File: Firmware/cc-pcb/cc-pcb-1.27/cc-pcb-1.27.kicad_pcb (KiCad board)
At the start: 2 copper layers, 39.4 x 36.8 mm, 20 parts, among them SW1 SRS

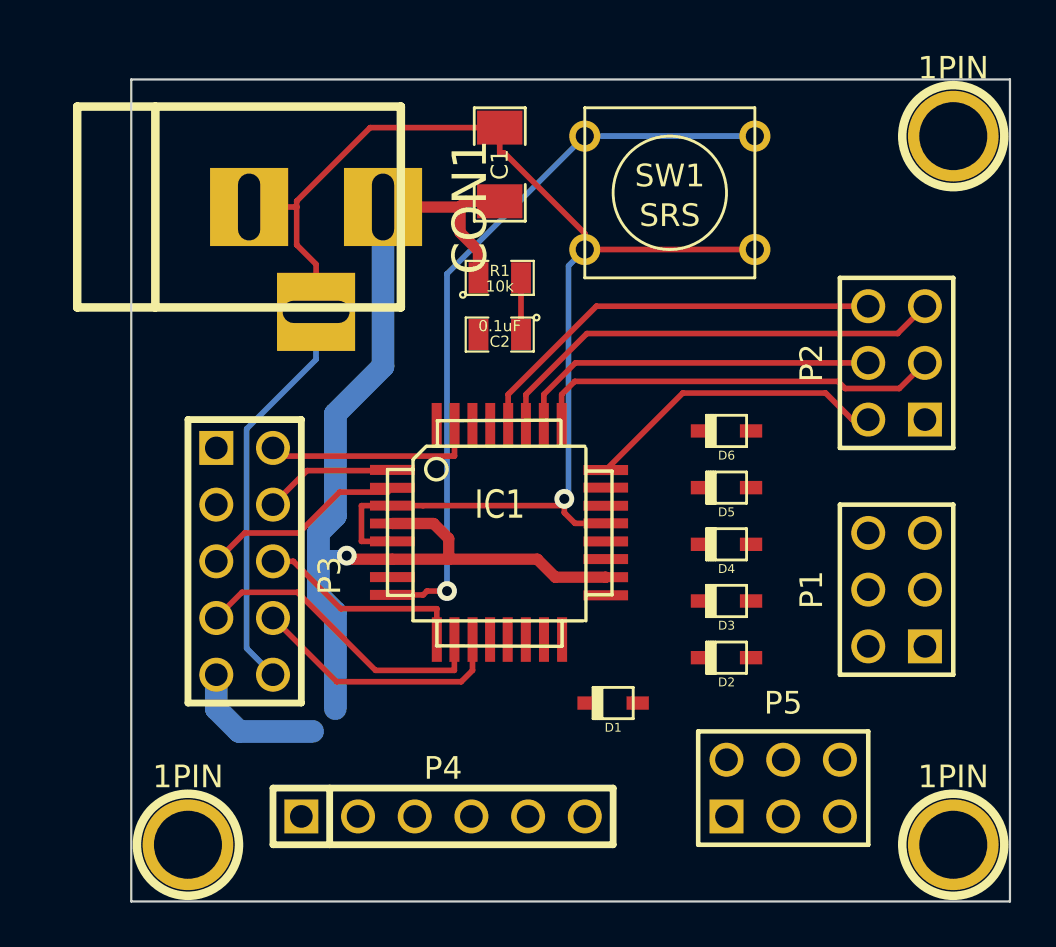
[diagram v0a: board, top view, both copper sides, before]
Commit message: added 1.27 pcb, 2mm pcb
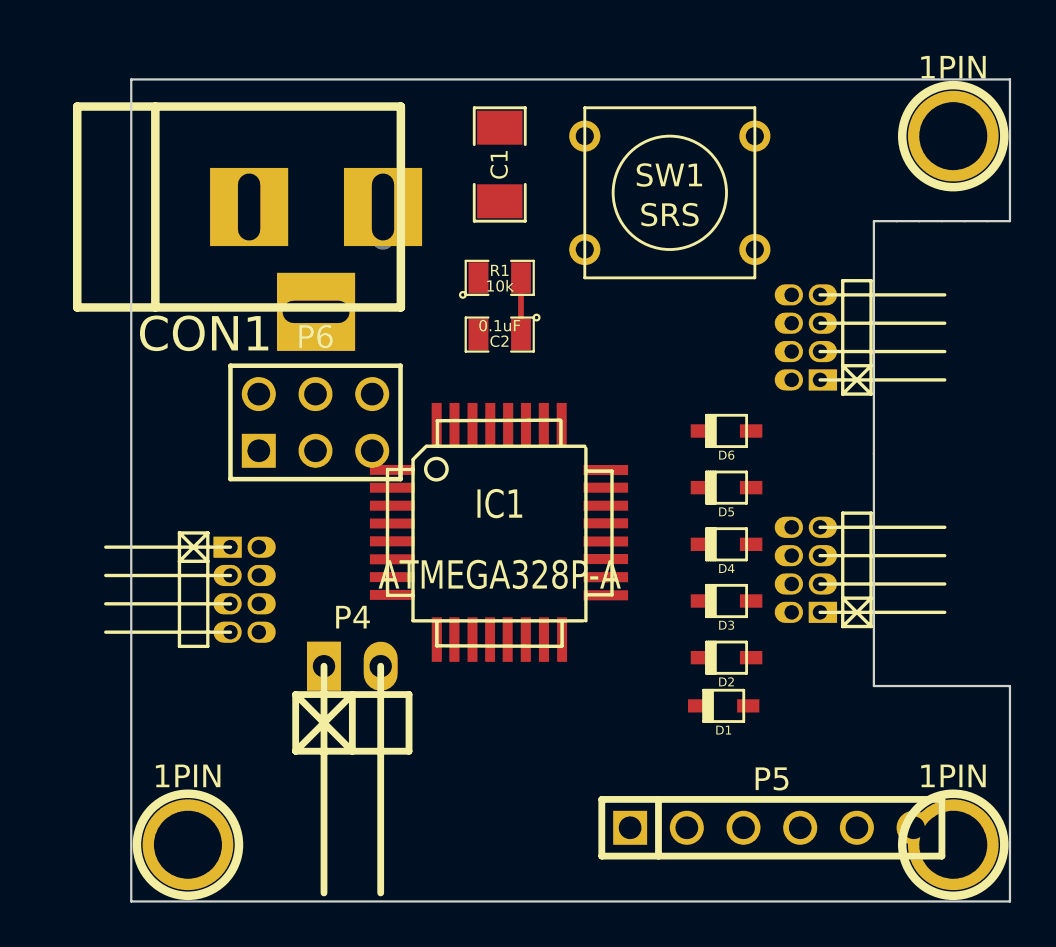
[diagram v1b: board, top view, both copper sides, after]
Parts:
- added P6: CONN_6, pin_array_3x2, F.Cu at (161.9, 87.8)
- CON1: value (none) -> BARREL_JACK
- IC1: value (none) -> ATMEGA328P-A
- P1, P2: value (none) -> CONN_6; footprint pin_array_3x2 -> pin_strip_1.27mm_4x2_90
- P3: value (none) -> CONN_8; footprint PIN_ARRAY_5x2 -> pin_strip_1.27mm_4x2_90
- P4: value (none) -> CONN_2; footprint PIN_ARRAY-6X1 -> pin_strip_2-90
- P5: value (none) -> CONN_6; footprint pin_array_3x2 -> PIN_ARRAY-6X1
- moved P4 7.86 mm to (163.6, 98.7)
- moved D1 4.95 mm to (180.2, 100.5)
- moved P2 4.22 mm to (183.9, 83.9)
- moved P1 4.16 mm to (183.9, 94.4)
- moved P5 1.85 mm to (182.4, 105.9)
- moved P3 1.27 mm to (158.8, 95.2)
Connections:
- C2 pad 1: N-0000029 -> N-000003
- C2 pad 2: N-0000030 -> N-000004
- D4 pad 2: N-0000017 (its old number) -> N-000008
- D5 pad 2: N-0000016 (its old number) -> N-000007
- D6 pad 2: N-0000015 (its old number) -> N-000006
- IC1 pad 15: N-0000017 (its old number) -> N-000008
- IC1 pad 16: N-0000016 (its old number) -> N-000007
- IC1 pad 17: N-0000015 (its old number) -> N-000006
- IC1 pad 29: N-0000029 -> N-000003
- IC1 pad 30: N-0000028 -> N-0000025
- IC1 pad 31: N-000007 -> N-000002
- P3 pad 1: N-0000028 -> N-0000025
- P3 pad 2: N-000007 -> N-000002
- P4 pad 1: N-0000030 -> VCC
- P4 pad 2: N-000007 -> GND
- P5 pad 1: N-0000016 (its old number) -> N-000004
- P5 pad 2: VCC -> N-000002
- P5 pad 3: N-0000015 (its old number) -> N-0000025
- P5 pad 4: N-0000017 (its old number) -> VCC
- P5 pad 5: N-0000029 -> GND
- R1 pad 2: N-0000029 -> N-000003
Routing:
- net GND: track 77.0 -> 0.00 mm, vias 1 -> 0
- net VCC: track 57.5 -> 2.82 mm, vias 1 -> 0
- net N-0000026: track 33.1 -> 0.00 mm, vias 1 -> 0
- net N-0000018: track 20.9 -> 0.00 mm
- net N-0000017: track 19.2 -> 0.00 mm
- net N-0000020: track 18.5 -> 0.00 mm
- net N-0000019: track 16.5 -> 0.00 mm
- net N-0000013: track 14.0 -> 0.00 mm
- net N-0000021: track 13.7 -> 0.00 mm
- net N-0000012: track 11.7 -> 0.00 mm
- net N-000007: track 9.88 -> 0.00 mm
- net N-0000014: track 9.60 -> 0.00 mm
- net N-0000015: track 9.26 -> 0.01 mm
- net N-0000016: track 5.99 -> 0.00 mm
- net N-000003: track 0.00 -> 2.54 mm
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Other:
- outline, holes or cut-outs redrawn

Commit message: moving parts around a bit
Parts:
- moved P5 3.39 mm to (179.1, 105.2)
- moved P4 3.30 mm to (164.5, 101.9), turned to 270 degrees
- moved CON1 1.71 mm to (157.5, 77.0)
- moved D4 1.15 mm to (179.2, 93.1)
- moved D6 1.15 mm to (179.2, 88.0)
- moved D1 1.15 mm to (179.1, 100.3)
- moved D2 1.15 mm to (179.2, 98.2)
- moved D3 1.15 mm to (179.2, 95.6)
- moved D5 1.15 mm to (179.2, 90.6)
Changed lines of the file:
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@@
   )
   (module sod323 (layer F.Cu)
-    (at 180.213 100.457 180)
+    (at 179.07 100.33 180)
     (descr SOD323)
     (fp_text reference D1 (at 0 -1.09982 180) (layer F.SilkS)
@@
   )
   (module sod323 (layer F.Cu)
-    (at 180.34 98.298 180)
+    (at 179.197 98.171 180)
     (descr SOD323)
     (fp_text reference D2 (at 0 -1.09982 180) (layer F.SilkS)
@@
   )
   (module sod323 (layer F.Cu)
-    (at 180.34 95.758 180)
+    (at 179.197 95.631 180)
     (descr SOD323)
     (fp_text reference D3 (at 0 -1.09982 180) (layer F.SilkS)
@@
   )
   (module sod323 (layer F.Cu)
-    (at 180.34 93.218 180)
+    (at 179.197 93.091 180)
     (descr SOD323)
     (fp_text reference D4 (at 0 -1.09982 180) (layer F.SilkS)
@@
   )
   (module sod323 (layer F.Cu)
-    (at 180.34 90.678 180)
+    (at 179.197 90.551 180)
     (descr SOD323)
     (fp_text reference D5 (at 0 -1.09982 180) (layer F.SilkS)
@@
   )
   (module sod323 (layer F.Cu)
-    (at 180.34 88.138 180)
+    (at 179.197 88.011 180)
     (descr SOD323)
     (fp_text reference D6 (at 0 -1.09982 180) (layer F.SilkS)
@@
   )
   (module BARREL_JACK (layer F.Cu)
-    (at 158.75 78.105)
+    (at 157.48 76.962)
     (descr "DC Barrel Jack")
     (tags "Power Jack")
@@
   )
   (module PIN_ARRAY-6X1 (layer F.Cu)
-    (at 182.372 105.918)
+    (at 179.07 105.156)
     (descr "Connecteur 6 pins")
     (tags "CONN DEV")
@@
   )
   (module pin_strip_2-90 (layer F.Cu)
-    (at 163.576 98.679)
+    (at 164.465 101.854 270)
     (descr "Pin strip 2pin 90")
     (tags "CONN DEV")
-    (fp_text reference P4 (at 0 -2.159) (layer F.SilkS)
+    (fp_text reference P4 (at 0 -2.159 270) (layer F.SilkS)
       (effects (font (size 1.016 1.016) (thickness 0.2032)))
     )
-    (fp_text value CONN_2 (at 0.254 -3.556) (layer F.SilkS) hide
+    (fp_text value CONN_2 (at 0.254 -3.556 270) (layer F.SilkS) hide
       (effects (font (size 1.016 0.889) (thickness 0.2032)))
     )
@@
     (fp_line (start 1.27 0) (end 1.27 10.16) (layer F.SilkS) (width 0.3048))
     (fp_line (start -2.54 3.81) (end -2.54 1.27) (layer F.SilkS) (width 0.3048))
-    (pad 1 thru_hole rect (at -1.27 0) (size 1.524 2.19964) (drill 1.00076)
+    (pad 1 thru_hole rect (at -1.27 0 270) (size 1.524 2.19964) (drill 1.00076)
       (layers *.Cu *.Mask F.SilkS)
       (net 31 VCC)
     )
-    (pad 2 thru_hole oval (at 1.27 0) (size 1.524 2.19964) (drill 1.00076)
+    (pad 2 thru_hole oval (at 1.27 0 270) (size 1.524 2.19964) (drill 1.00076)
       (layers *.Cu *.Mask F.SilkS)
       (net 1 GND)
@@
   (segment (start 171.3484 97.4852) (end 171.348 97.4852) (width 0.254) (layer F.Cu) (net 30))
   (segment (start 174.9298 94.6912) (end 174.93 94.6912) (width 0.508) (layer F.Cu) (net 31))
-  (segment (start 164.95 78.105) (end 164.95 79.5159) (width 1.016) (layer B.Cu) (net 31))
-  (segment (start 164.9501 79.5158) (end 164.9501 78.105) (width 0.508) (layer B.Cu) (net 31))
-  (segment (start 164.95 79.5159) (end 164.9501 79.5158) (width 0.508) (layer B.Cu) (net 31))
+  (segment (start 163.68 76.962) (end 163.68 78.3729) (width 1.016) (layer B.Cu) (net 31) (status 30))
+  (segment (start 163.6801 78.3728) (end 163.6801 76.962) (width 0.508) (layer B.Cu) (net 31) (status 30))
+  (segment (start 163.68 78.3729) (end 163.6801 78.3728) (width 0.508) (layer B.Cu) (net 31) (status 30))
 )
